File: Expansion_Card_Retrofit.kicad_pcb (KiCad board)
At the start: 8 copper layers, 24 x 27.3 mm, 189 parts, among them J1 Conn_02x02_Odd_Even, J3 5024302030, J4 Conn_02x02_Odd_Even, P1 1054440011, U1 RP2350_60QFN, U10 TMP110D, U2 CCGM1A1, U3 TVS0500DRV, U4 W25Q16JLUXIG TR, U5 USB3740B-AI2, U6 TPS7A2033PDQNR, U7 TPSM82822SILR, U8 TPSM82822SILR, U9 ISM330DHCX, Y1 S3A2505-100.000-L-X1-R, Y2 ABM8-272-T3

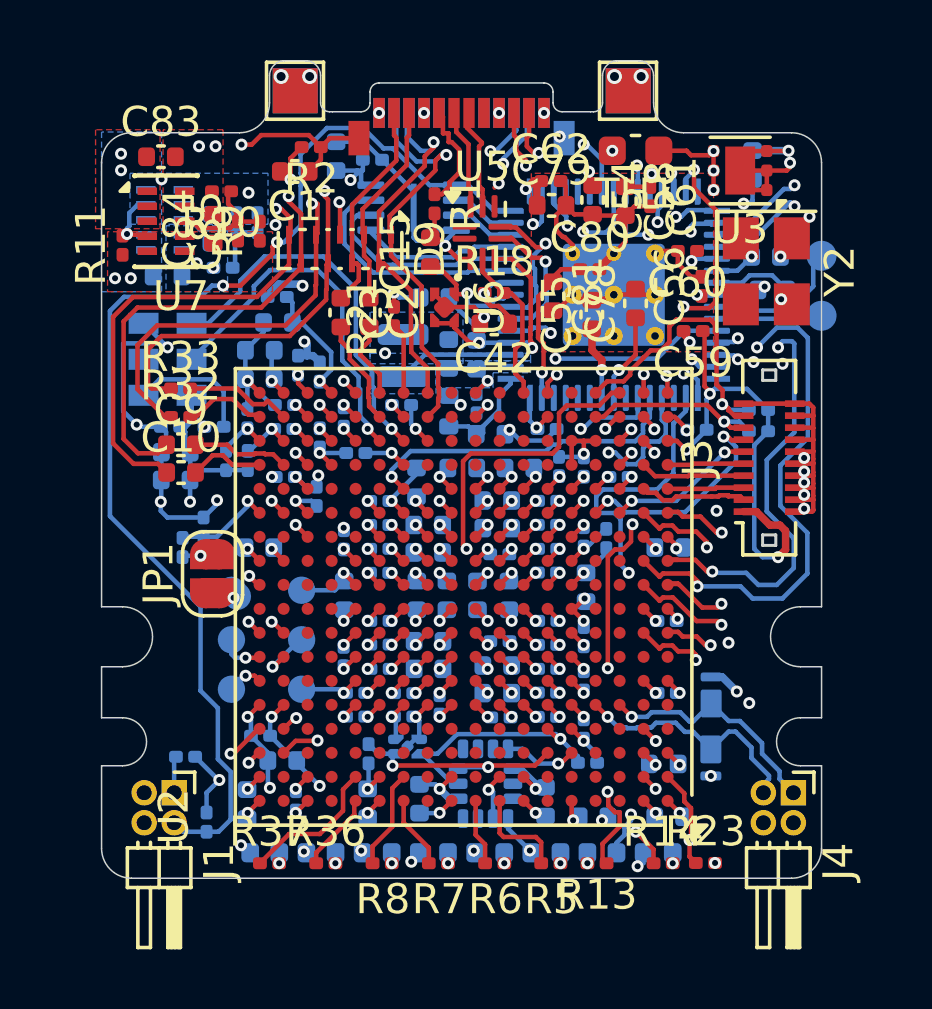
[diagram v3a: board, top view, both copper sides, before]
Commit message: update on layout first drc done
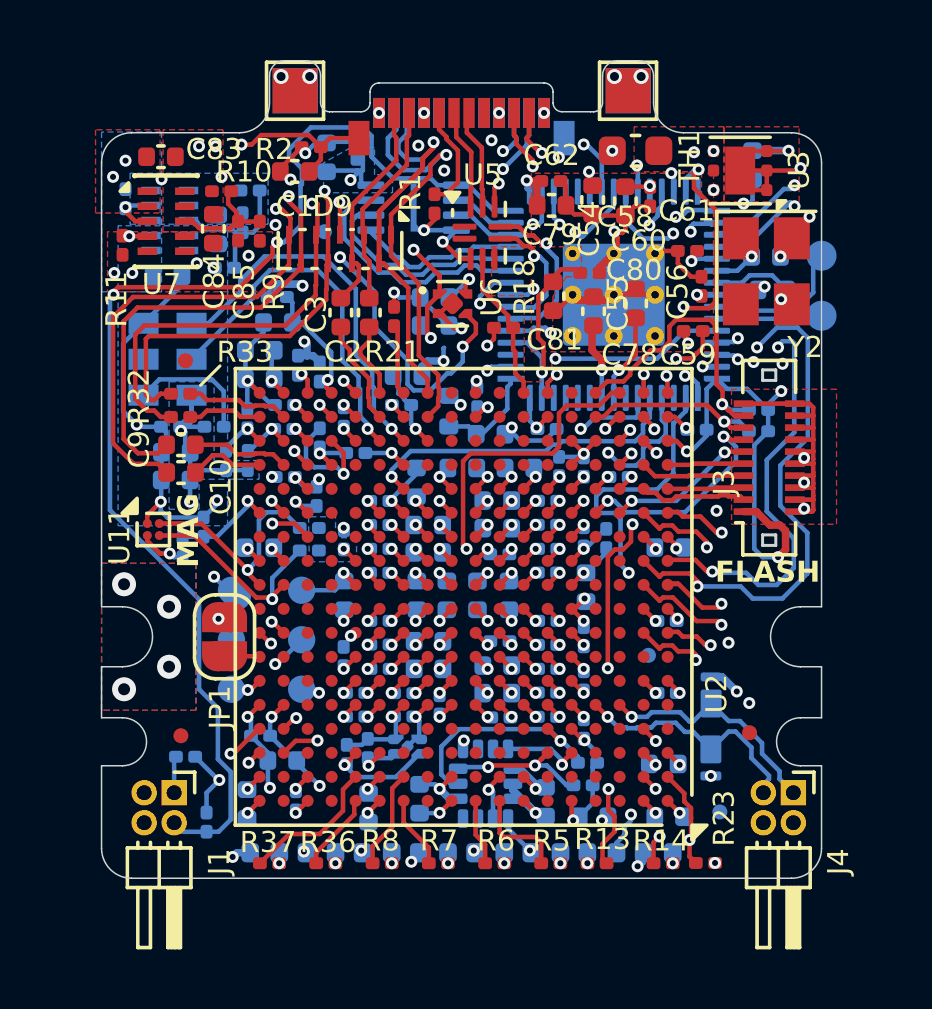
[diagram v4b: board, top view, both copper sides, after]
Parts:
- removed C4, C5: 4u7, Capacitor_SMD:C_0402_1005Metric
- removed L1: 3u3, RP2350_60QFN_minimal:L_pol_2016
- added FID1: Fiducial, Fiducial:Fiducial_0.5mm_Mask1mm, B.Cu at (146.2, 147.1)
- added FID2: Fiducial, Fiducial:Fiducial_0.5mm_Mask1mm, B.Cu at (148.6, 152.3)
- added FID3: Fiducial, Fiducial:Fiducial_0.5mm_Mask1mm, B.Cu at (135.4, 133.0)
- added FID4: Fiducial, Fiducial:Fiducial_0.5mm_Mask1mm, F.Cu at (130.8, 137.3)
- added FID5: Fiducial, Fiducial:Fiducial_0.5mm_Mask1mm, F.Cu at (149.6, 149.7)
- added FID6: Fiducial, Fiducial:Fiducial_0.5mm_Mask1mm, F.Cu at (130.6, 149.8)
- added R40: 100K, Resistor_SMD:R_0201_0603Metric, B.Cu at (128.8, 131.9)
- added R41: 5K1, Resistor_SMD:R_0201_0603Metric, B.Cu at (134.9, 142.9)
- added R42: 5K1, Resistor_SMD:R_0201_0603Metric, B.Cu at (134.9, 143.6)
- added R43: 5K1, Resistor_SMD:R_0201_0603Metric, B.Cu at (136.9, 150.2)
- added R44: 5K1, Resistor_SMD:R_0201_0603Metric, B.Cu at (136.2, 150.4)
- added U11: MMC5633NJL, Package_BGA:WLP-4_0.86x0.86mm_P0.4mm, F.Cu at (129.7, 142.9)
- C15, C42: moved to B.Cu
- R24: value 316K -> 84K5
- U1: value RP2350_60QFN -> RP2350A
- moved R19 7.23 mm to (144.1, 151.4), turned to 180 degrees
- moved C42 3.37 mm to (138.2, 137.8)
- moved C15 2.45 mm to (139.1, 136.1), turned to 0 degrees
- moved JP1 2.14 mm to (132.1, 146.5), turned to -90 degrees
- moved R18 1.20 mm to (141.4, 136.2)
- moved C87 1.10 mm to (132.9, 131.6), turned to 0 degrees
- moved C46 0.64 mm to (136.5, 130.2), turned to 90 degrees
- moved C47 0.32 mm to (135.5, 130.5)
- moved U6 0.30 mm to (139.7, 135.4), turned to 0 degrees
- moved C43 0.21 mm to (140.5, 138.5)
- moved C88 0.20 mm to (131.9, 132.9)
- moved R24 0.20 mm to (132.7, 132.7)
- moved U8 0.18 mm to (130.3, 132.6)
- moved R33 0.18 mm to (130.6, 138.4)
- moved C18 0.15 mm to (136.9, 152.2)
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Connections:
- net /K8 renamed /K5
- C100 pad 1: +1V -> +1V1
- C101 pad 1: +1V -> +1V1
- C102 pad 1: +1V -> +1V1
- C103 pad 1: +1V -> +1V1
- C104 pad 1: +1V -> +1V1
- C105 pad 1: +1V -> +1V1
- C106 pad 1: +1V -> +1V1
- C107 pad 1: +1V -> +1V1
- C108 pad 1: +1V -> +1V1
- C109 pad 1: +1V -> +1V1
- C110 pad 1: +1V -> +1V1
- C111 pad 1: +1V -> +1V1
- C112 pad 1: +1V -> +1V1
- C113 pad 1: +1V -> +1V1
- C114 pad 1: +1V -> +1V1
- C115 pad 1: +1V -> +1V1
- C116 pad 1: +1V -> +1V1
- C117 pad 1: +1V -> +1V1
- C53 pad 1: +1V -> +1V1
- C63 pad 1: +1V -> +1V1
- C64 pad 1: +1V -> +1V1
- C82 pad 1: +1V -> +1V1
- C87 pad 1: +1V -> +1V1
- C88 pad 1: +1V -> +1V1
- C89 pad 1: +1V -> +1V1
- C90 pad 1: +1V -> +1V1
- C91 pad 1: +1V -> +1V1
- C92 pad 1: +1V -> +1V1
- C93 pad 1: +1V -> +1V1
- C94 pad 1: +1V -> +1V1
- C95 pad 1: +1V -> +1V1
- C96 pad 1: +1V -> +1V1
- C97 pad 1: +1V -> +1V1
- C98 pad 1: +1V -> +1V1
- C99 pad 1: +1V -> +1V1
- JP1 pad 2: +2V5 -> /MIC_DOUT
- MK1 pad 5: /MIC_DOUT -> Net-(JP1-A)
- MK1 pad 6: Net-(JP1-A) -> +2V5
- R11 pad 2: /power_supply/PG -> /power_supply/PG_2V5
- R16 pad 1: +1V -> +1V1
- R24 pad 1: +1V -> +1V1
- U1 pad 48: Net-(U1-VREG_LX) -> unconnected-(U1-VREG_LX-Pad48)
- U1 pad 49: VBUS -> +3V3
- U10 pad 2: /SCL0 -> /SCL2
- U10 pad 4: /SDA0 -> /SDA2
- U2 pad C13: unconnected-(U2C-IO_NB_B6-PadC13) -> /SDA2
- U2 pad C14: unconnected-(U2C-IO_NB_B8-PadC14) -> /SCL2
- U2 pad F9: +1V -> +1V1
- U2 pad G10: +1V -> +1V1
- U2 pad G12: +1V -> +1V1
- U2 pad G6: +1V -> +1V1
- U2 pad G8: +1V -> +1V1
- U2 pad H11: +1V -> +1V1
- U2 pad H13: +1V -> +1V1
- U2 pad H7: +1V -> +1V1
- U2 pad H9: +1V -> +1V1
- U2 pad J10: +1V -> +1V1
- U2 pad J12: +1V -> +1V1
- U2 pad J6: +1V -> +1V1
- U2 pad J8: +1V -> +1V1
- U2 pad K11: +1V -> +1V1
- U2 pad K13: +1V -> +1V1
- U2 pad K17: unconnected-(U2D-IO_EA_B2-PadK17) -> /SDA1
- U2 pad K18: /power_supply/PG -> /SCL1
- U2 pad K7: +1V -> +1V1
- U2 pad K9: +1V -> +1V1
- U2 pad L10: +1V -> +1V1
- U2 pad L12: +1V -> +1V1
- U2 pad L6: +1V -> +1V1
- U2 pad L8: +1V -> +1V1
- U2 pad M11: +1V -> +1V1
- U2 pad M13: +1V -> +1V1
- U2 pad M7: +1V -> +1V1
- U2 pad M9: +1V -> +1V1
- U2 pad N10: +1V -> +1V1
- U2 pad N6: +1V -> +1V1
- U2 pad N8: +1V -> +1V1
- U2 pad P16: +1V -> +1V1
- U2 pad T14: +1V -> +1V1
- U2 pad T16: +1V -> +1V1
- U2 pad U12: +1V -> +1V1
- U2 pad V17: +1V -> +1V1
- U5 pad 5: VBUS -> +3V3
- U6 pad 3: VBUS -> /power_supply/PG_2V5
- U7 pad 3: VBUS -> /power_supply/PG_1V1
- U7 pad 4: /power_supply/PG -> /power_supply/PG_2V5
- U8 pad 4: /power_supply/PG -> /power_supply/PG_1V1
- U8 pad 5: +1V -> +1V1
- U8 pad 6: +1V -> +1V1
- U8 pad 7: +1V -> +1V1
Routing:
- net VBUS: track 43.5 -> 22.1 mm, vias 7 -> 6
- net +1V: track 21.0 -> 0.00 mm, vias 36 -> 0
- net /power_supply/PG: track 18.2 -> 0.00 mm, vias 2 -> 0
- net /power_supply/PG_2V5: track 0.00 -> 17.9 mm, vias 0 -> 3
- net GND: track 129.1 -> 138.7 mm, vias 119 -> 128
- net /SCL1: track 0.00 -> 7.87 mm, vias 0 -> 1
- net /SDA1: track 0.00 -> 7.27 mm, vias 0 -> 1
- net +2V5: track 80.5 -> 87.5 mm, vias 68 -> 74
- net +1V1: track 32.7 -> 26.3 mm, vias 5 -> 40
- net /RX1_P: track 12.0 -> 17.5 mm
- net Net-(U1-VREG_LX): track 3.89 -> 0.00 mm
- net /SCL2: track 0.00 -> 3.54 mm, vias 0 -> 1
- net /~{RST}: track 66.6 -> 69.5 mm
- net /SDA0: track 7.90 -> 5.43 mm
- net /power_supply/PG_1V1: track 0.00 -> 1.88 mm, vias 0 -> 1
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- added copper zone on In4.Cu, net +1V1
- added copper zone on B.Cu, net +2V5
- added copper zone on F.Cu, net +3V3
- added copper zone on In5.Cu, net Net-(P1-VBUS-PadA4)
- added copper zone on In4.Cu, net VBUS
- added copper zone on In5.Cu, net VBUS
- removed copper zone on B.Cu, net +1V
- removed copper zone on In4.Cu, net GND
- removed copper zone on B.Cu, net Net-(U1-VREG_LX)
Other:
- board text added: "0"
- board text added: "0 mm"
- board text added: "0.01 mm"
- board text added: "0.0152 mm"
- board text added: "0.02"
- board text added: "0.025 mm"
- board text added: "0.035 mm"
- board text added: "0.04 mm"
- board text added: "0.1 mm"
- board text added: "0.2 mm"
- board text added: "1"
- board text added: "3.3"
- board text added: "4.5"
- board text added: "B.Cu"
- board text added: "B.Mask"
- board text added: "B.Paste"
- board text added: "B.Silkscreen"
- board text added: "BOTTOM designators"
- board text added: "Bottom Silk Screen"
- board text added: "Bottom Solder Mask"
- board text added: "Bottom Solder Paste"
- board text added: "Color"
- board text added: "D ~{F} 0 1 2 3 4 5"
- board text added: "Dielectric"
- board text added: "Epsilon R"
- board text added: "F.Cu"
- board text added: "F.Mask"
- board text added: "F.Paste"
- board text added: "F.Silkscreen"
- board text added: "FLASH"
- board text added: "FR4"
- board text added: "FR4 natural"
- board text added: "Green"
- board text added: "IMU"
- board text added: "In1.Cu(GND)"
- board text added: "In2.Cu"
- board text added: "In3.Cu(GND)"
- board text added: "In4.Cu(1V1)"
- board text added: "In5.Cu(2V5)"
- board text added: "In6.Cu(GND)"
- board text added: "Layer Name"
- board text added: "Loss Tangent"
- board text added: "MAG"
- board text added: "Material"
- board text added: "Not specified"
- board text added: "Thickness (mm)"
- board text added: "Top Silk Screen"
- board text added: "Top Solder Mask"
- board text added: "Top Solder Paste"
- board text added: "Type"
- board text added: "White"
- board text added: "copper"
- board text added: "core"
- board text added: "prepreg"
- board text removed: "0.1524 mm / 0.1016 mm"
- board text removed: "0.2000 mm"
- board text removed: "0.7964 mm"
- board text removed: "8"
- board text removed: "ENIG"
- board text removed: "Yes"

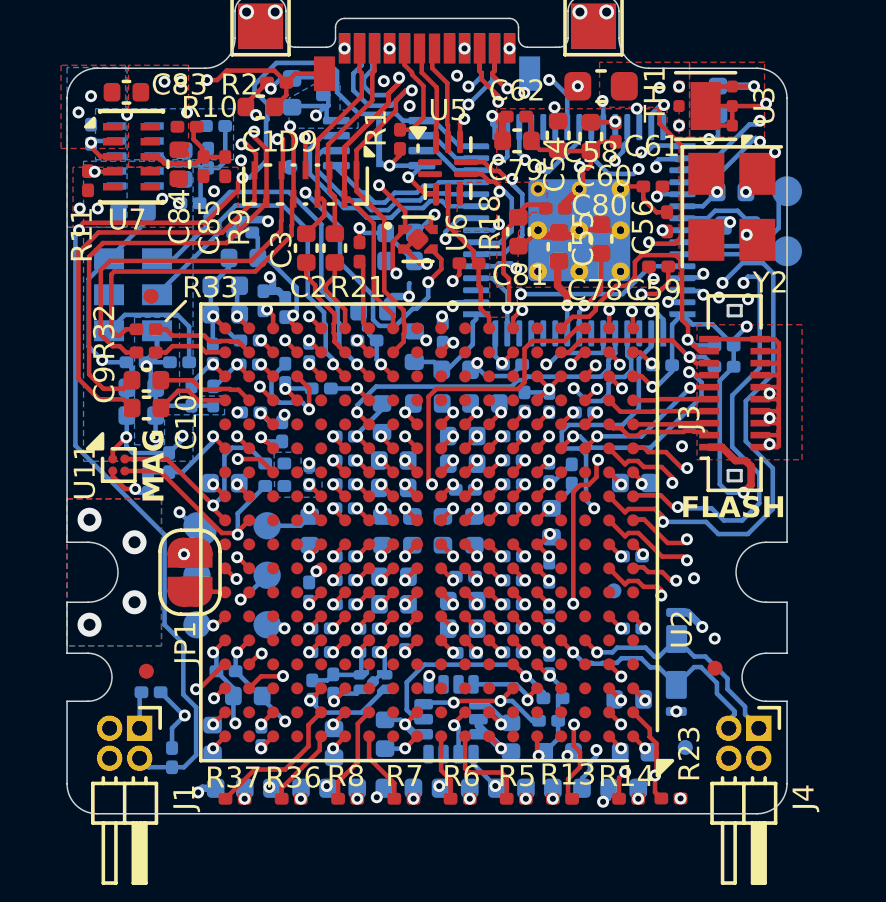
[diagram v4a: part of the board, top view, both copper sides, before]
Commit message: start to switch to stm32
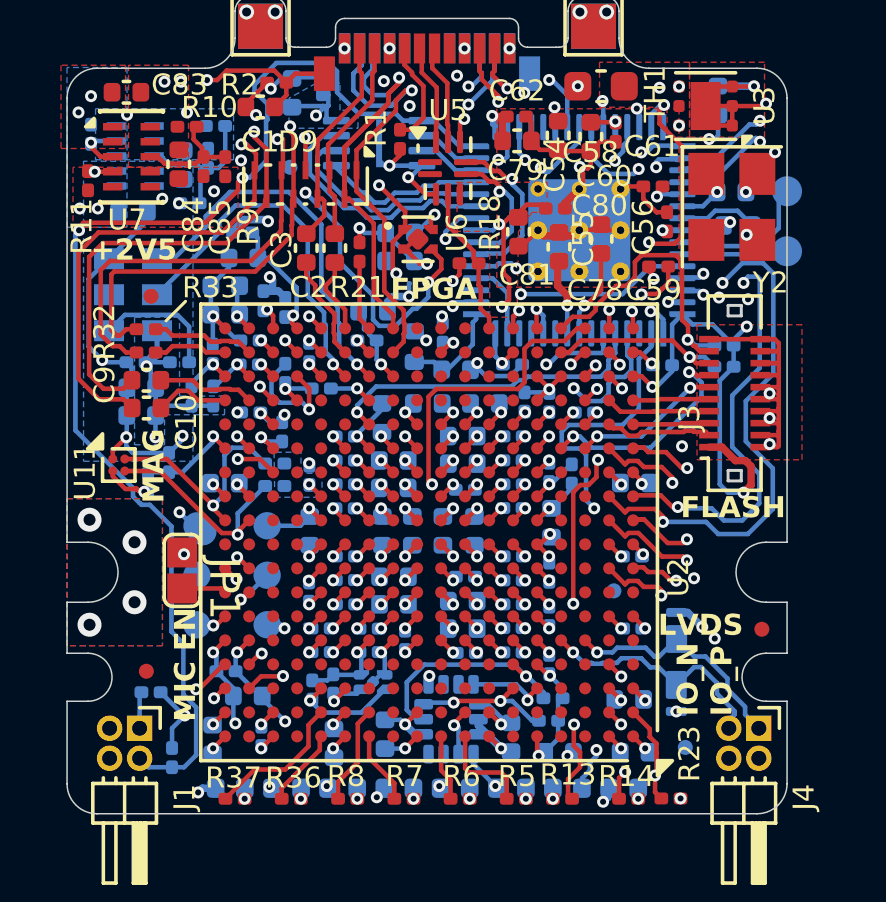
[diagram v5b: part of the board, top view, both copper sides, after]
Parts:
- JP1: footprint Jumper:SolderJumper-2_P1.3mm_Open_RoundedPad1.0x1.5mm -> ProjectLibrary:Jumper_open
- moved FID5 2.03 mm to (151.2, 148.4)
- moved JP1 0.27 mm to (131.8, 146.4)
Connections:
- U1 pad 41: unconnected-(U1-GPIO27_ADC1-Pad41) -> /CC_CFG_CTRL_RECFG
- U2 pad V5: unconnected-(U2E-IO_SA_B0-PadV5) -> /CC_CFG_CTRL_RECFG
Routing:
- net /CC_CFG_CTRL_RECFG: track 0.00 -> 1.57 mm, vias 0 -> 1
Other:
- board text added: "+1V1"
- board text added: "+2V5"
- board text added: "FPGA"
- board text added: "IO_N IO_P"
- board text added: "LVDS"
- board text added: "MIC EN"
- board text added: "SWCLK"
- board text added: "SWD"
